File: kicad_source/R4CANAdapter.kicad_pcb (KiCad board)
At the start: 2 copper layers, 21 x 25 mm, 18 parts, among them CN1 CONN_01X05, CN2 691322310004, CN3 GH_SM04B-GHS-TB, CN4 GH_SM04B-GHS-TB, U1 TCAN332GDR

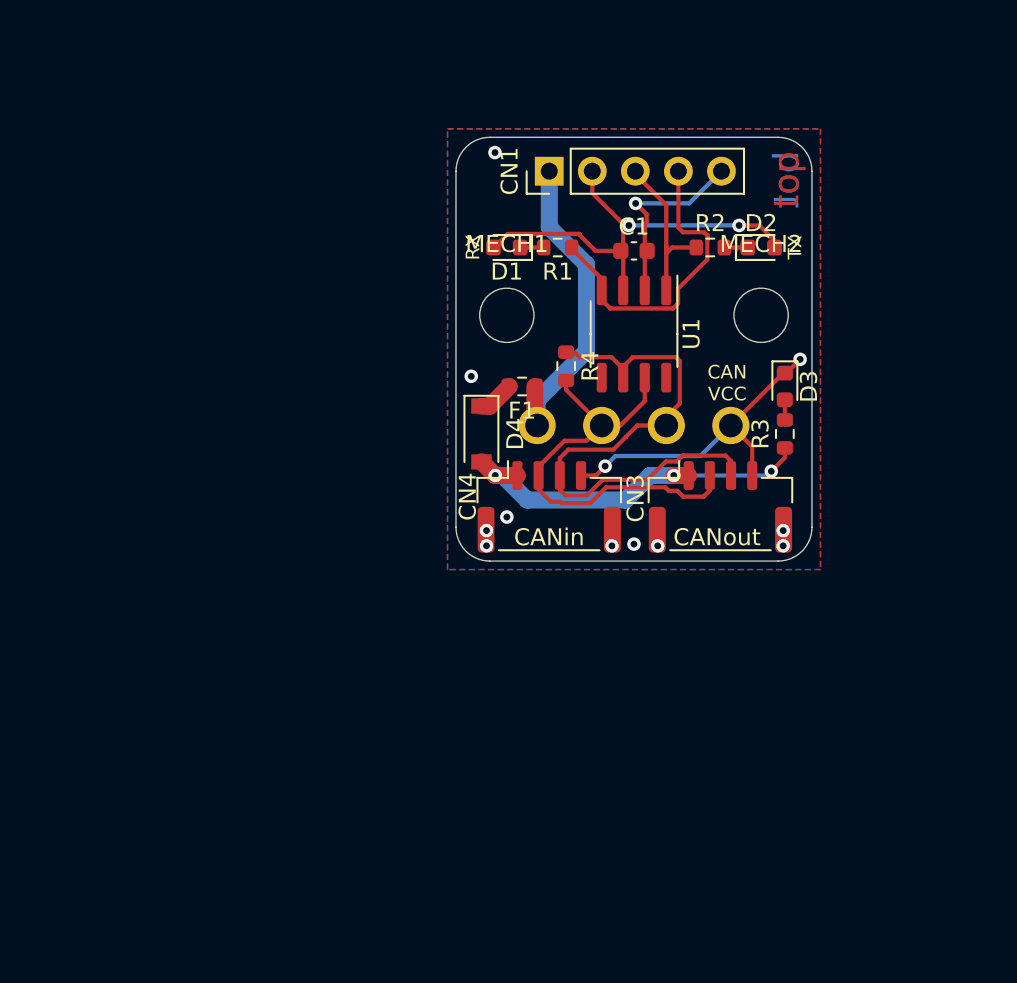
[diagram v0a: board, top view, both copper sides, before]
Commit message: added Arduino Uno connector
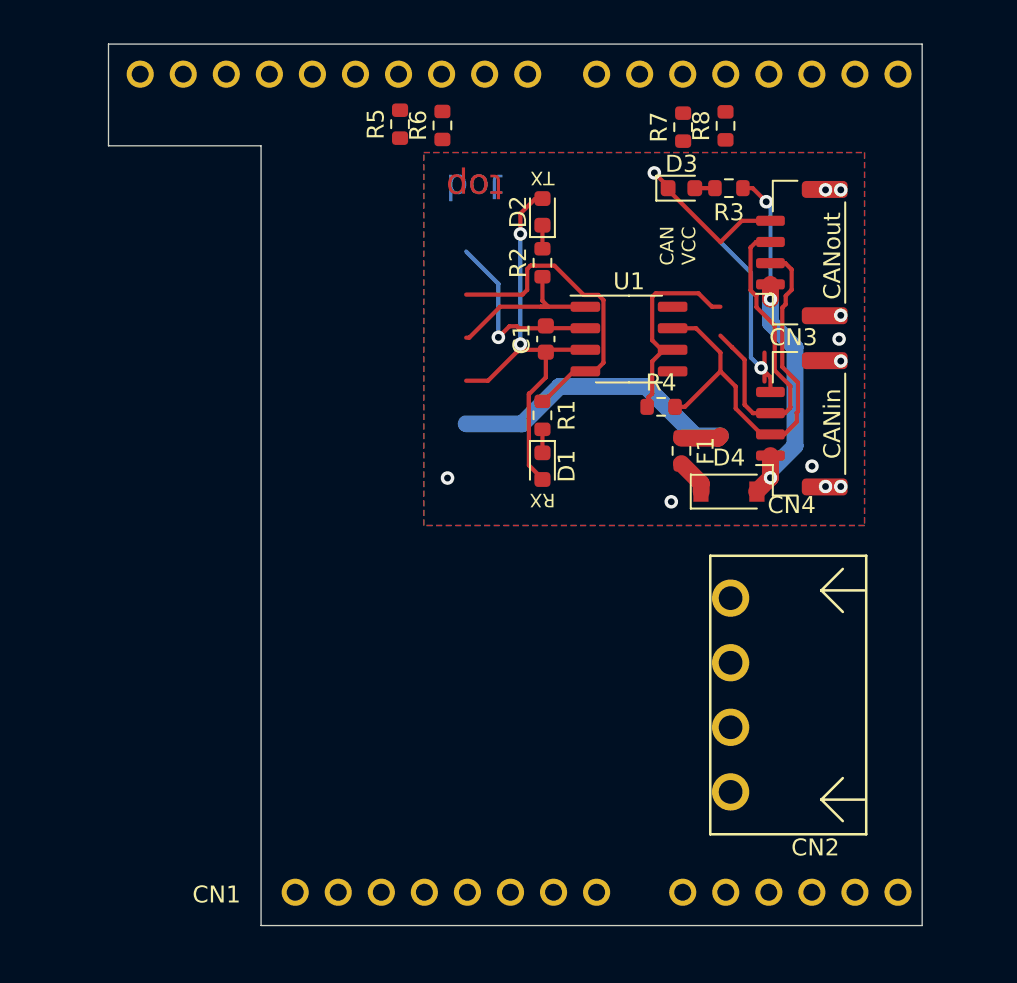
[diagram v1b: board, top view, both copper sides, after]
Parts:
- removed MECH1, MECH2: MHP_3.2_5.0, MountingHole:MountingHole_3.2mm_M3
- added R5: DNI, Resistor_SMD:R_0603_1608Metric, F.Cu at (134.2, 90.7)
- added R6: DNI, Resistor_SMD:R_0603_1608Metric, F.Cu at (136.7, 90.8)
- added R7: 0R, Resistor_SMD:R_0603_1608Metric, F.Cu at (150.9, 90.9)
- added R8: 0R, Resistor_SMD:R_0603_1608Metric, F.Cu at (153.4, 90.8)
- CN1: footprint Connector_PinHeader_2.54mm:PinHeader_1x05_P2.54mm_Vertical -> generationmake:ARDUINO
- CN2: moved to F.Cu
- moved CN1 62.2 mm to (100.1, 138.6), turned to 0 degrees
- moved CN2 16.9 mm to (153.7, 124.4), turned to 90 degrees
- moved CN3 15.7 mm to (157.9, 98.3), turned to 90 degrees
- moved CN4 15.7 mm to (157.9, 108.4), turned to 90 degrees
- moved D4 15.0 mm to (153.6, 112.4), turned to 0 degrees
- moved R3 14.9 mm to (153.6, 94.5), turned to 180 degrees
- moved D3 13.2 mm to (150.8, 94.5), turned to 0 degrees
- moved D1 13.1 mm to (142.6, 110.9), turned to -90 degrees
- moved D2 13.1 mm to (142.6, 95.9), turned to 90 degrees
- moved F1 10.1 mm to (150.8, 110.0), turned to -90 degrees
- moved R1 9.94 mm to (142.6, 107.9), turned to -90 degrees
- moved R2 9.94 mm to (142.6, 98.9), turned to 90 degrees
- moved C1 7.35 mm to (142.8, 103.4), turned to 90 degrees
- moved R4 6.09 mm to (149.6, 107.4), turned to 0 degrees
- moved L1 3.68 mm to (145.4, 103.4), turned to -90 degrees
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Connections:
- CN1 pad 1: +5V -> unconnected-(CN1-Pad1)
- CN1 pad 2: +3V3 -> unconnected-(CN1-Pad2)
- CN1 pad 3: /CAN_TX -> unconnected-(CN1-Pad3)
- CN1 pad 4: /CAN_RX -> /CAN_TX_MINIMA
- CN1 pad 5: GND -> /CAN_RX_MINIMA
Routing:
- net GND: track 30.6 -> 32.3 mm
- net /CANL: track 33.8 -> 32.1 mm
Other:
- board size 21 x 25 mm -> 48 x 52 mm

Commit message: added I2C and eeprom
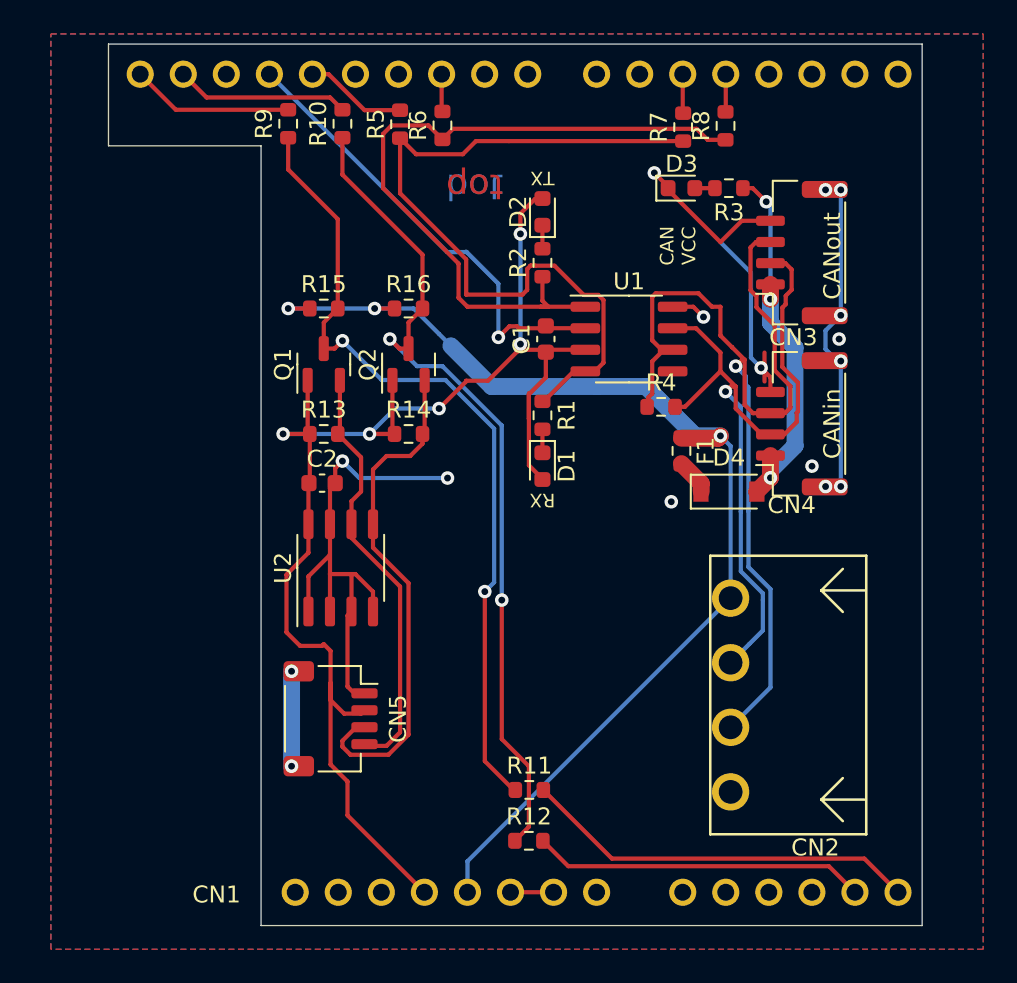
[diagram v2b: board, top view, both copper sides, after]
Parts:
- added C2: 100nF, Capacitor_SMD:C_0603_1608Metric, F.Cu at (129.6, 111.9)
- added CN5: SM04B-SRSS-TB, Connector_JST:JST_SH_SM04B-SRSS-TB_1x04-1MP_P1.00mm_Horizontal, F.Cu at (130.1, 125.8)
- added Q1: 2N7002, Package_TO_SOT_SMD:SOT-23, F.Cu at (129.7, 104.9)
- added Q2: 2N7002, Package_TO_SOT_SMD:SOT-23, F.Cu at (134.7, 104.9)
- added R10: 0R, Resistor_SMD:R_0603_1608Metric, F.Cu at (130.8, 90.7)
- added R11: DNI, Resistor_SMD:R_0603_1608Metric, F.Cu at (141.8, 130.0)
- added R12: DNI, Resistor_SMD:R_0603_1608Metric, F.Cu at (141.8, 133.0)
- added R13: 10k, Resistor_SMD:R_0603_1608Metric, F.Cu at (129.7, 109.0)
- added R14: 10k, Resistor_SMD:R_0603_1608Metric, F.Cu at (134.7, 109.0)
- added R15: 10k, Resistor_SMD:R_0603_1608Metric, F.Cu at (129.7, 101.6)
- added R16: 10k, Resistor_SMD:R_0603_1608Metric, F.Cu at (134.7, 101.6)
- added R9: 0R, Resistor_SMD:R_0603_1608Metric, F.Cu at (127.6, 90.7)
- added U2: 24LC64, Package_SO:SO-8_3.9x4.9mm_P1.27mm, F.Cu at (130.7, 116.9)
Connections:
- CN1 pad 14: unconnected-(CN1-Pad14) -> GND
- CN1 pad 16: unconnected-(CN1-Pad16) -> /ARDUINO_SDA
- CN1 pad 17: unconnected-(CN1-Pad17) -> /ARDUINO_SCL
- CN1 pad 18: unconnected-(CN1-Pad18) -> /R4_SCL
- CN1 pad 19: unconnected-(CN1-Pad19) -> /R4_SDA
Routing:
- net +3V3: track 27.5 -> 84.4 mm, vias 2 -> 5
- net GND: track 32.3 -> 84.6 mm, vias 7 -> 9
- net /I2C_SDA: track 0.00 -> 50.3 mm, vias 0 -> 2
- net /I2C_SCL: track 0.00 -> 48.7 mm, vias 0 -> 2
- net +5V: track 19.5 -> 67.0 mm, vias 0 -> 3
- net /CAN_TX: track 10.1 -> 42.8 mm
- net /I2C_SDA_3V: track 0.00 -> 30.4 mm
- net /CAN_RX: track 18.2 -> 46.5 mm
- net /I2C_SCL_3V: track 0.00 -> 25.3 mm
- net /CANL: track 32.1 -> 56.7 mm, vias 0 -> 1
- net /R4_SCL: track 0.00 -> 23.4 mm
- net /R4_SDA: track 0.00 -> 19.7 mm
- net /CANH: track 26.3 -> 44.7 mm, vias 0 -> 1
- net /MP: track 0.00 -> 18.4 mm
- net /ARDUINO_SDA: track 0.00 -> 10.3 mm
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
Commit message: beautified layout
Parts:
- moved D3 20.7 mm to (145.5, 114.5)
- moved R3 20.5 mm to (149.0, 114.5)
- moved D1 13.5 mm to (145.1, 97.6), turned to 0 degrees
- moved R1 10.3 mm to (141.7, 97.6), turned to 0 degrees
- moved R4 4.94 mm to (152.5, 103.4), turned to 90 degrees
- moved R2 4.39 mm to (141.7, 94.6), turned to 0 degrees
- moved C2 3.00 mm to (132.6, 111.9)
- moved Q1 3.00 mm to (132.7, 104.9)
- moved Q2 3.00 mm to (137.7, 104.9)
- moved R13 3.00 mm to (132.7, 109.0)
- moved R14 3.00 mm to (137.7, 109.0)
- moved R15 3.00 mm to (132.7, 101.6)
- moved R16 3.00 mm to (137.7, 101.6)
- moved U2 3.00 mm to (133.7, 116.9)
- moved CN2 2.88 mm to (152.1, 122.0)
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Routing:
- net GND: track 84.6 -> 68.3 mm, vias 9 -> 8
- net +3V3: track 84.4 -> 75.5 mm, vias 5 -> 3
- net /CAN_RX: track 46.5 -> 40.5 mm
- net /CANL: track 56.7 -> 51.8 mm
- net /CAN_TX: track 42.8 -> 39.6 mm
- net +5V: track 67.0 -> 64.4 mm
- net /CANVCC: track 22.7 -> 20.4 mm, vias 3 -> 2
- net /CANH: track 44.7 -> 42.4 mm
- net /I2C_SDA: track 50.3 -> 52.6 mm
- net /I2C_SCL: track 48.7 -> 49.9 mm
- net Net-(D3-Pad2): track 1.30 -> 1.89 mm
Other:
- board size 48 x 52 mm -> 47.5 x 51 mm

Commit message: used real jumpers
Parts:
- removed R10, R7, R8, R9: 0R, Resistor_SMD:R_0603_1608Metric
- removed R11, R12, R5, R6: DNI, Resistor_SMD:R_0603_1608Metric
- added JP1: Jumper_3_Bridged12, Connector_PinHeader_2.54mm:PinHeader_1x03_P2.54mm_Vertical, F.Cu at (141.3, 91.4)
- added JP2: Jumper_3_Bridged12, Connector_PinHeader_2.54mm:PinHeader_1x03_P2.54mm_Vertical, F.Cu at (141.3, 94.2)
- added JP3: Jumper_3_Bridged12, Connector_PinHeader_2.54mm:PinHeader_1x03_P2.54mm_Vertical, F.Cu at (125.6, 91.5)
- added JP4: Jumper_3_Bridged12, Connector_PinHeader_2.54mm:PinHeader_1x03_P2.54mm_Vertical, F.Cu at (125.6, 94.3)
- moved D1 5.38 mm to (150.5, 97.8)
- moved D2 5.38 mm to (150.5, 94.8)
- moved L1 5.38 mm to (150.1, 102.0)
- moved R1 5.38 mm to (147.1, 97.8)
- moved R2 5.38 mm to (147.1, 94.8)
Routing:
- net /R4_SDA: track 19.7 -> 68.6 mm, vias 0 -> 1
- net /R4_SCL: track 23.4 -> 71.9 mm, vias 0 -> 1
- net /I2C_SDA: track 52.6 -> 17.8 mm, vias 2 -> 0
- net /I2C_SCL: track 49.9 -> 17.7 mm, vias 2 -> 0
- net /CAN_TX: track 39.6 -> 16.6 mm
- net /CAN_RX: track 40.5 -> 25.7 mm
- net /CAN_TX_MINIMA: track 2.65 -> 16.0 mm
- net /CAN_RX_MINIMA: track 2.70 -> 11.2 mm
- net /CAN_TX_WIFI: track 2.22 -> 7.29 mm
- net /CAN_RX_WIFI: track 6.05 -> 8.72 mm
- net GND: track 68.3 -> 70.5 mm
- net +3V3: track 75.5 -> 77.0 mm
- net /ARDUINO_SCL: track 9.60 -> 8.25 mm
- net /ARDUINO_SDA: track 10.3 -> 11.1 mm

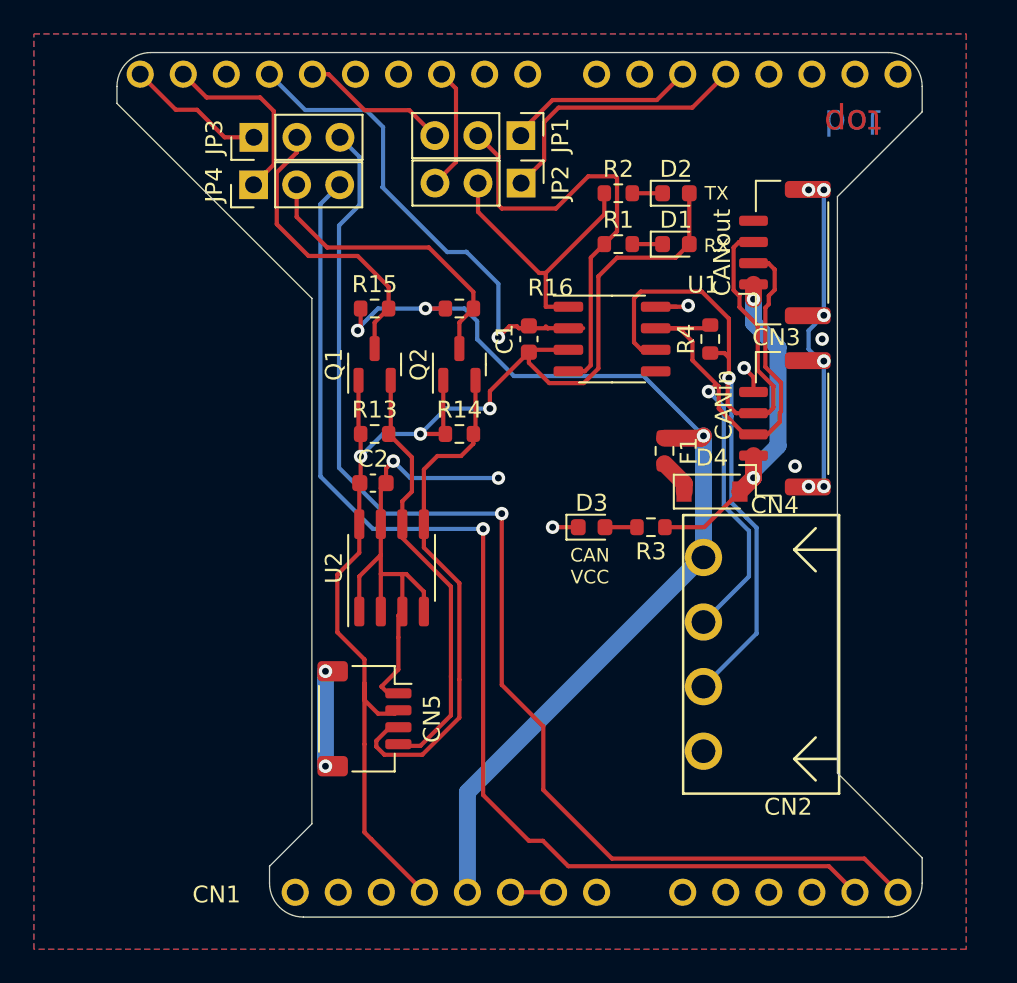
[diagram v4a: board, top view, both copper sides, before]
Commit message: switched I2C eeprom and CAN driver to the 5V domain
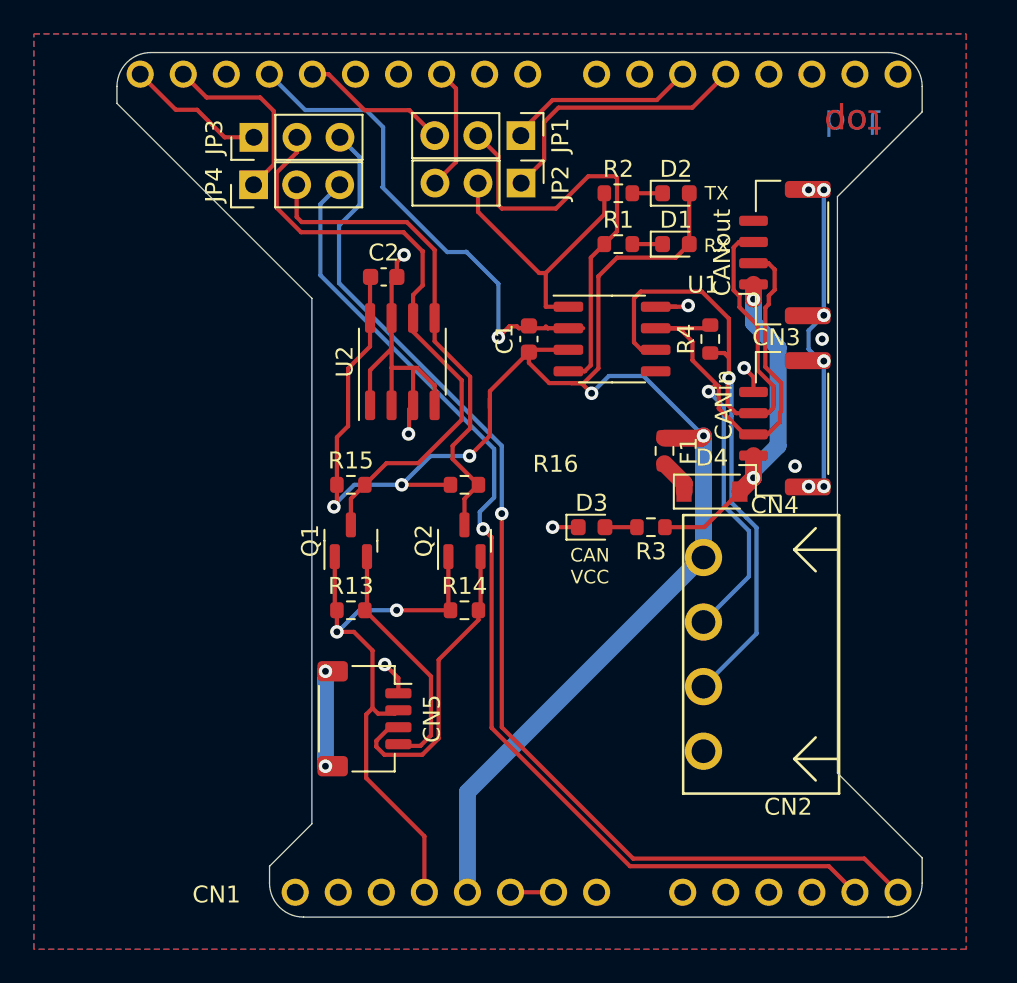
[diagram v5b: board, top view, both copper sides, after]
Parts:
- U1: value TCAN332GDR -> MCP2551-I/SN
- moved C2 12.2 mm to (133.2, 99.7)
- moved U2 12.2 mm to (134.3, 104.7)
- moved R13 10.5 mm to (131.3, 119.4)
- moved R15 10.5 mm to (131.3, 112.0)
- moved Q1 10.5 mm to (131.3, 115.3)
- moved R14 10.4 mm to (138.0, 119.4)
- moved R16 10.4 mm to (138.0, 112.0)
- moved Q2 10.4 mm to (138.0, 115.3)
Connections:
- C1 pad 1: +3V3 -> +5V
- C2 pad 1: +3V3 -> +5V
- D1 pad 2: +3V3 -> +5V
- D2 pad 2: +3V3 -> +5V
- U1 pad 3: +3V3 -> +5V
- U2 pad 5: /I2C_SDA_3V -> /I2C_SDA
- U2 pad 6: /I2C_SCL_3V -> /I2C_SCL
- U2 pad 8: +3V3 -> +5V
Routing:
- net +3V3: track 77.0 -> 35.1 mm, vias 3 -> 2
- net +5V: track 64.0 -> 104.1 mm, vias 3 -> 5
- net /I2C_SCL: track 17.7 -> 35.7 mm
- net /I2C_SDA_3V: track 30.8 -> 18.0 mm
- net /I2C_SDA: track 17.8 -> 29.3 mm
- net /I2C_SCL_3V: track 25.7 -> 14.4 mm
- net GND: track 70.5 -> 61.6 mm, vias 8 -> 9
- net /R4_SDA: track 68.6 -> 62.8 mm
- net /R4_SCL: track 71.9 -> 67.2 mm

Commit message: added bypass resistors for I2C circuit
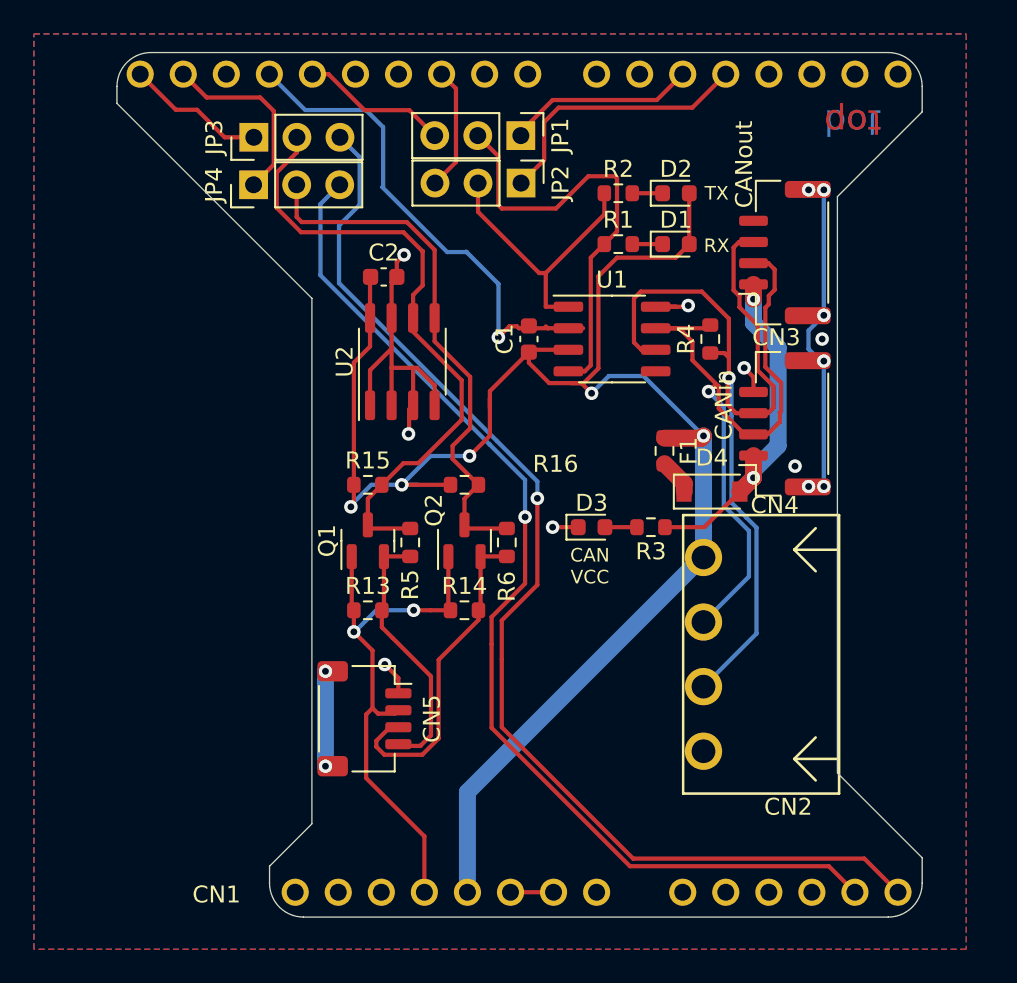
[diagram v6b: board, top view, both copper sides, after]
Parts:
- added R5: DNI, Resistor_SMD:R_0603_1608Metric, F.Cu at (134.8, 115.4)
- added R6: DNI, Resistor_SMD:R_0603_1608Metric, F.Cu at (140.5, 115.4)
- moved Q1 1.00 mm to (132.3, 115.3)
- moved R13 1.00 mm to (132.3, 119.4)
- moved R15 1.00 mm to (132.3, 112.0)
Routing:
- net /I2C_SDA: track 29.3 -> 31.9 mm
- net +3V3: track 35.1 -> 33.1 mm
- net /R4_SCL: track 67.2 -> 68.9 mm
- net /I2C_SCL: track 35.7 -> 37.3 mm
- net /I2C_SDA_3V: track 18.0 -> 19.6 mm
- net /I2C_SCL_3V: track 14.4 -> 15.6 mm
- net /R4_SDA: track 62.8 -> 63.8 mm
